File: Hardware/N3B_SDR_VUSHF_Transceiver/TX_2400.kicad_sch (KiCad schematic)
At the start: 123 parts, among them J1 PATCH01, J2 ADF4360+AD8346 SHIELD, J3 SP5189 SHIELD, J4 PATCH02, J5 Line In/PTT, J6 MIC/PTT, J7 SMA RF OUT, SW1 RESET, U1 RP2040_PICO, U2 LM324, U3 LM4562, U4 LM4562, U5 AD8346ARUZ-REEL7, U6 SPF5189Z, U7 ADF4360-0BCP, U8 LM1117-5.0, U9 LM1117-3.3, Y1 10Mhz

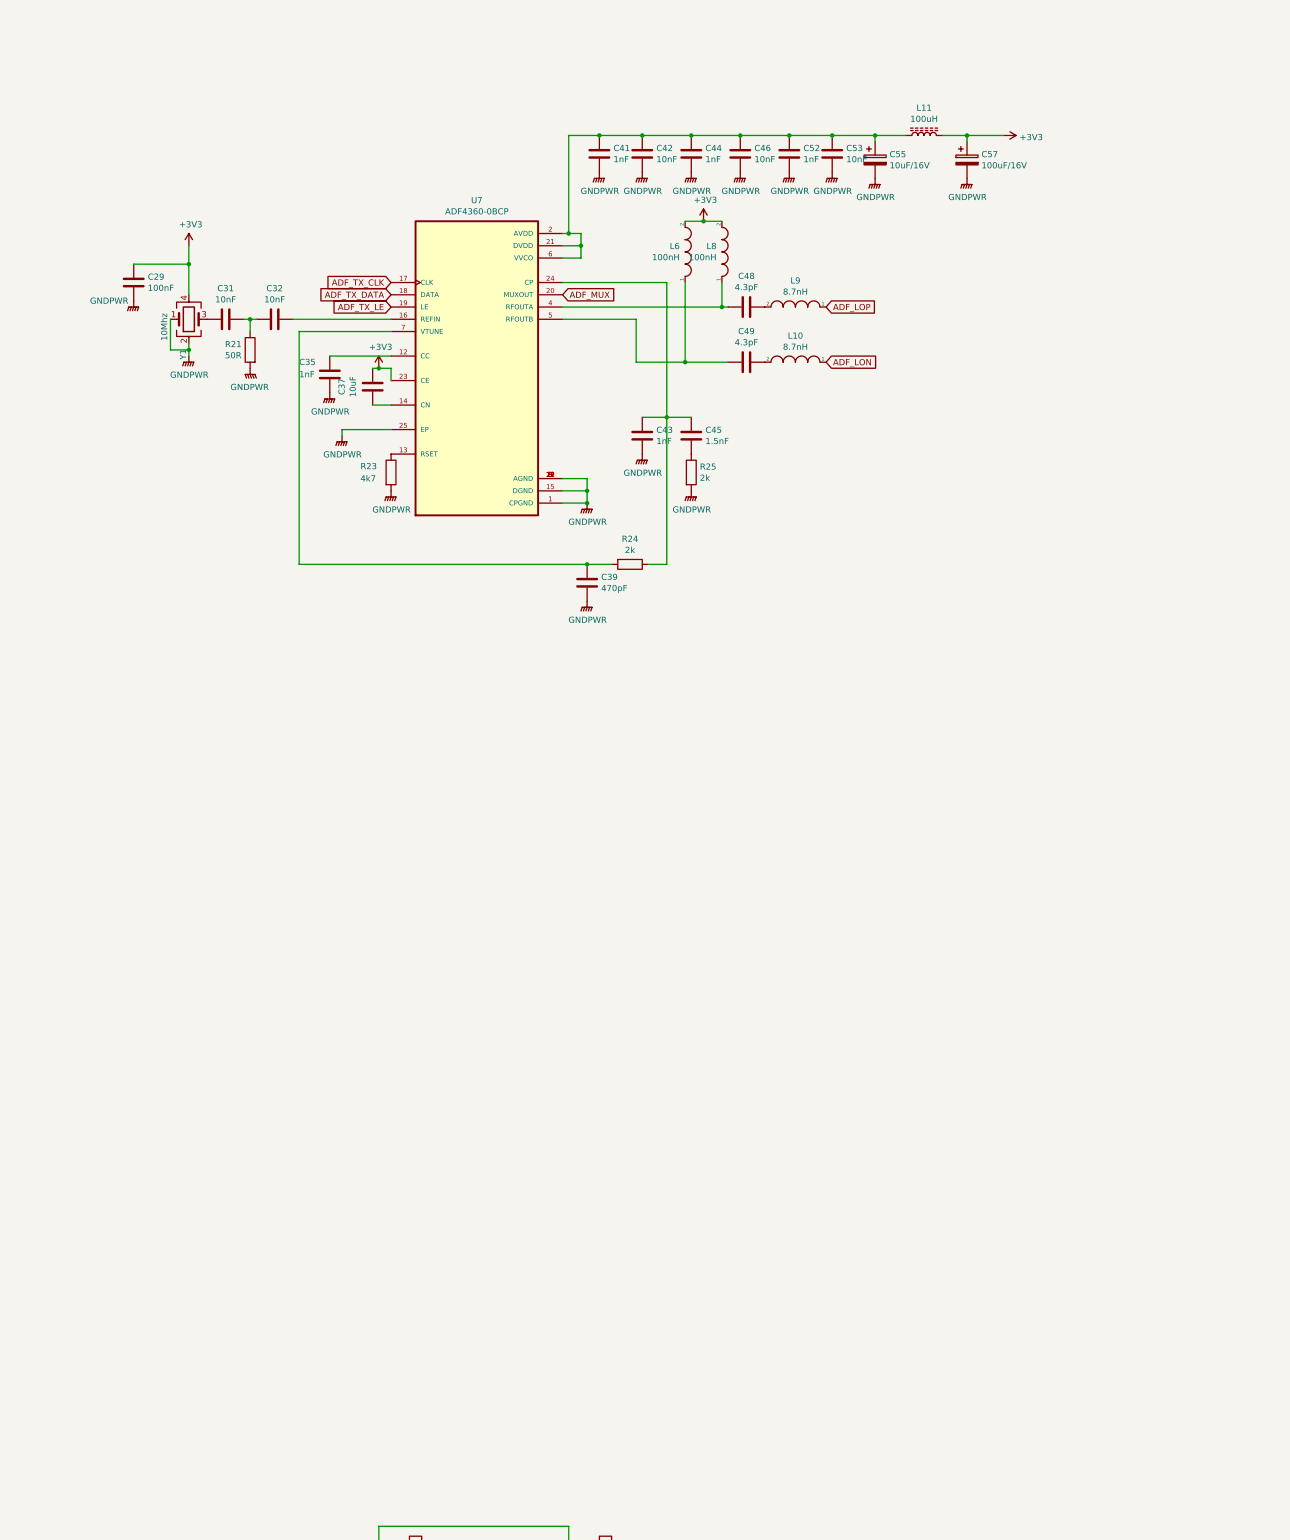
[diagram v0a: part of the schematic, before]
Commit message: TX Synth modified to LMX2581
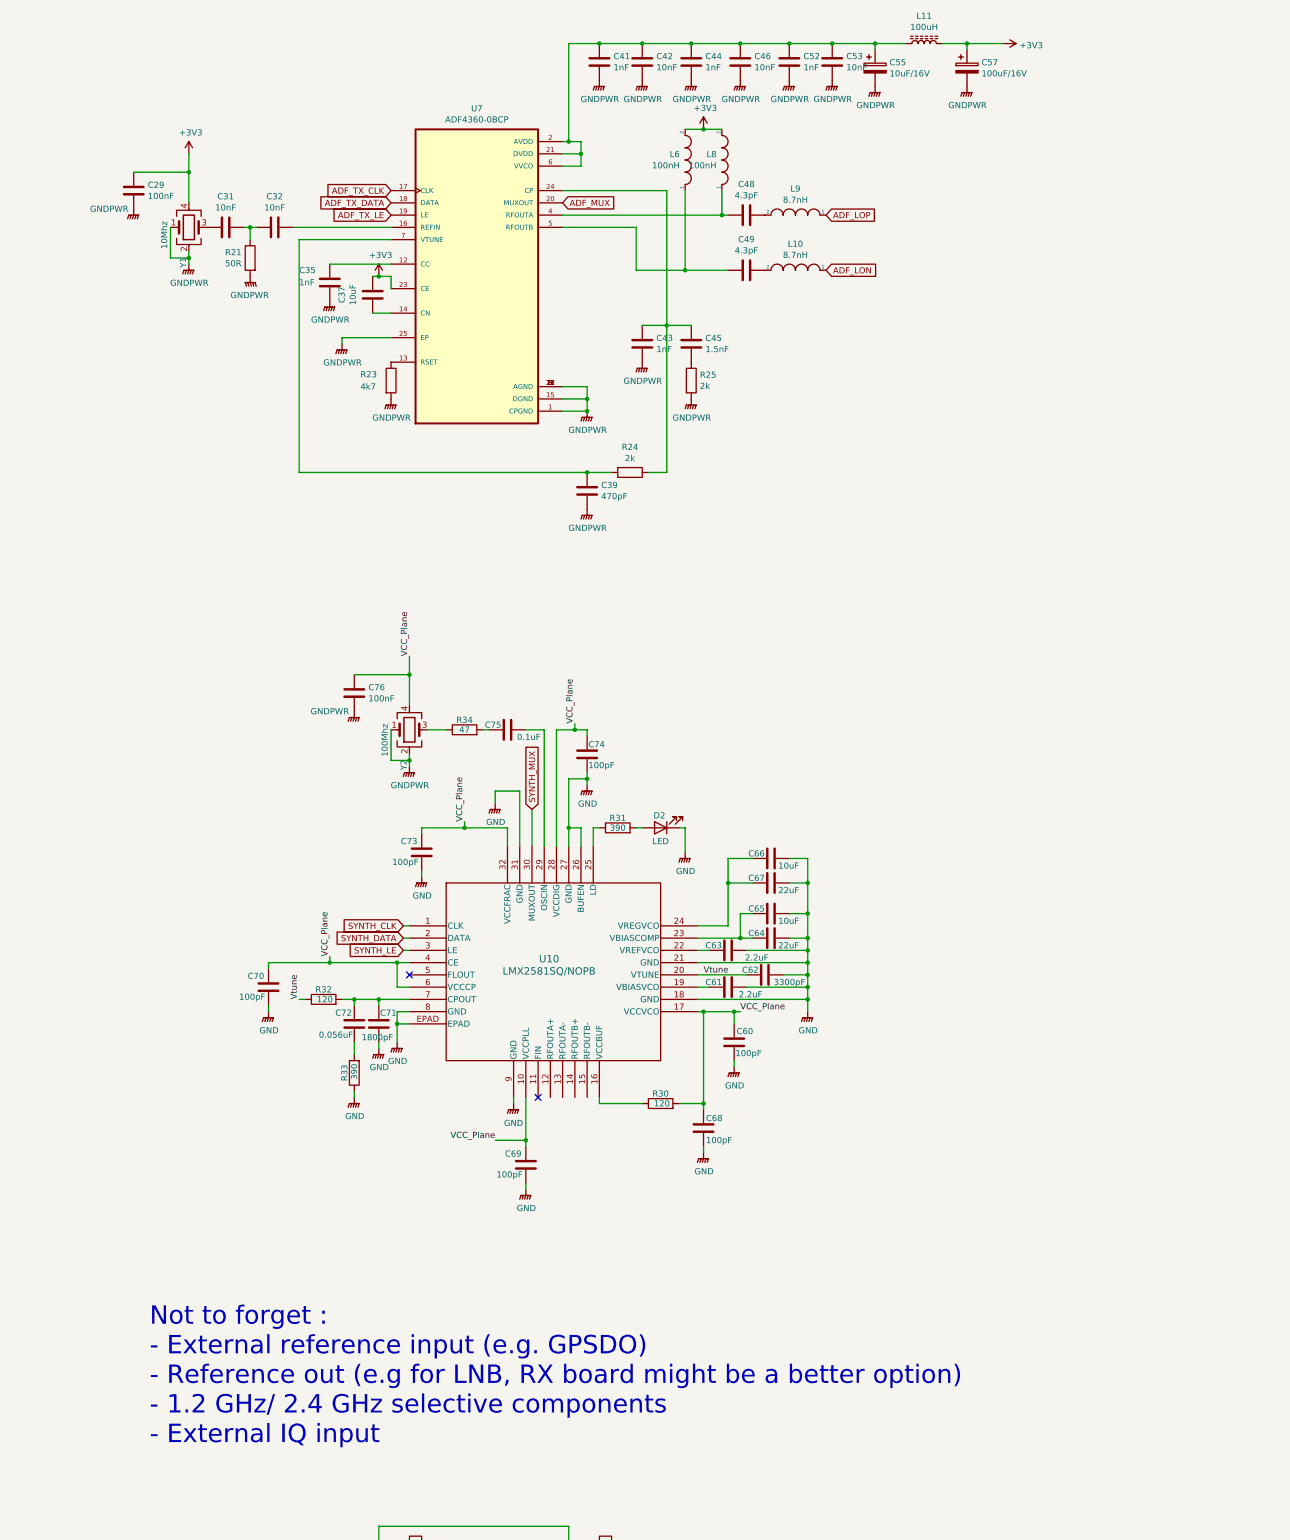
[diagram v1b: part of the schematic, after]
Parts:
- added C60, C68, C69, C70, C73, C74: 100pF, Capacitor_SMD:C_0805_2012Metric, symbol Device:C
- added C61, C63: 2.2uF, Capacitor_SMD:C_0805_2012Metric, symbol Device:C
- added C62: 3300pF, Capacitor_SMD:C_0805_2012Metric, symbol Device:C
- added C64, C67: 22uF, Capacitor_SMD:C_0805_2012Metric, symbol Device:C
- added C65, C66: 10uF, Capacitor_SMD:C_0805_2012Metric, symbol Device:C
- added C71: 1800pF, Capacitor_SMD:C_0805_2012Metric, symbol Device:C
- added C72: 0.056uF, Capacitor_SMD:C_0805_2012Metric, symbol Device:C
- added C75: 0.1uF, Capacitor_SMD:C_0805_2012Metric, symbol Device:C
- added C76: 100nF, Capacitor_SMD:C_0805_2012Metric, symbol Device:C
- added D2: LED, symbol Device:LED
- added R30, R32: 120, Resistor_SMD:R_0805_2012Metric, symbol Device:R
- added R31, R33: 390, Resistor_SMD:R_0805_2012Metric, symbol Device:R
- added R34: 47, Resistor_SMD:R_0805_2012Metric, symbol Device:R
- added U10: LMX2581SQ/NOPB, footprints:LMX2581, symbol LMX2581:LMX2581SQ_NOPB
- added Y2: 100Mhz, Crystal:Crystal_SMD_SeikoEpson_FA238V-4Pin_3.2x2.5mm, symbol Device:Crystal_GND24
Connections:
- net GNDPWR: now also C76.2, Y2.1, Y2.2
- new net: R30.1, U10.16 (VCCBUF)
- new net: C61.1, U10.19 (VBIASVCO)
- new net: C63.1, U10.22 (VREFVCO)
- new net: C64.1, C65.1, U10.23 (VBIASCOMP)
- new net: C66.1, C67.1, U10.24 (VREGVCO)
- new net: R31.1, U10.25 (LD)
- new net: C75.2, U10.29 (OSCIN)
- new net: C71.1, C72.1, R32.2, U10.7 (CPOUT)
- new net: R34.1, Y2.3
- new net: C75.1, R34.2
- new net: C72.2, R33.2
- new net: D2.2 (A), R31.2
- new net GND: C60.2, C61.2, C62.2, C63.2, C64.2, C65.2, C66.2, C67.2, C68.2, C69.2, C70.2, C71.2, C73.2, C74.2, D2.1 (K), R33.1, U10.18 (GND), U10.21 (GND), U10.26 (BUFEN), U10.27 (GND), U10.31 (GND), U10.8 (GND), U10.9 (GND), U10.EPAD
- new net SYNTH_CLK: U10.1 (CLK)
- new net SYNTH_DATA: U10.2 (DATA)
- new net SYNTH_LE: U10.3 (LE)
- new net SYNTH_MUX: U10.30 (MUXOUT)
- new net VCC_Plane: C60.1, C68.1, C69.1, C70.1, C73.1, C74.1, C76.1, R30.2, U10.10 (VCCPLL), U10.17 (VCCVCO), U10.28 (VCCDIG), U10.32 (VCCFRAC), U10.4 (CE), U10.6 (VCCCP), Y2.4
- new net Vtune: C62.1, R32.1, U10.20 (VTUNE)
- no-connect marks 0 -> 2
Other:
- note added: "Not to forget : - External reference input (e.g. GPSDO) - Reference out (e.g for LNB, RX board might be a better option) - 1.2 GHz/ 2.4 GHz selective components - External IQ input"
- moved on the sheet: C29, C31, C32, C35, C37, C39, C41, C42, C43, C44, C45, C46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

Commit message: local oscillators replaced with TI
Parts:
- removed C32, C42, C46: 10nF, Capacitor_SMD:C_0805_2012Metric, symbol Device:C
- removed C35, C41, C43, C44: 1nF, Capacitor_SMD:C_0805_2012Metric, symbol Device:C
- removed C37: 10uF, Capacitor_SMD:C_0805_2012Metric, symbol Device:C
- removed C39: 470pF, Capacitor_SMD:C_0805_2012Metric, symbol Device:C
- removed C45: 1.5nF, Capacitor_SMD:C_0805_2012Metric, symbol Device:C
- removed C48, C49: 4.3pF, Capacitor_SMD:C_0805_2012Metric, symbol Device:C
- removed L10, L9: 8.7nH, Inductor_SMD:L_0603_1608Metric, symbol QO100_TX-rescue:INDUCTOR-pspice
- removed L6, L8: 100nH, Inductor_SMD:L_0603_1608Metric, symbol QO100_TX-rescue:INDUCTOR-pspice
- removed R25: 2k, Resistor_SMD:R_0805_2012Metric, symbol Device:R
- removed U7: ADF4360-0BCP, ADF4360-5BCP:ADF4360SEDA, symbol QO100_TX-rescue:ADF4360-5BCP-ADF4360-5BCP
- removed Y1: 10Mhz, Crystal:Crystal_SMD_SeikoEpson_FA238V-4Pin_3.2x2.5mm, symbol Device:Crystal_GND24
- added J8: SMA REF IN, Connector_Coaxial:SMA_Samtec_SMA-J-P-X-ST-EM1_EdgeMount, symbol Connector:Conn_Coaxial
- added JP1: ~, symbol Jumper:Jumper_2_Bridged
- added JP2: ~, symbol Jumper:Jumper_2_Open
- C29: value 100nF -> 10pF
- C31: value 10nF -> 10pF
- C76: value 100nF -> 1uF
- R21: value 50R -> 10
- R23: value 4k7 -> 18
- R24: value 2k -> 33
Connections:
- net ADF_MUX is gone; now on net SYNTH_MUX: U1.6 (GP4)
- net ADF_TX_CLK is gone; now on net SYNTH_CLK: U1.14 (GP10)
- net ADF_TX_DATA is gone; now on net SYNTH_DATA: U1.15 (GP11)
- net ADF_TX_LE is gone; now on net SYNTH_LE: U1.17 (GP13)
- net +3V3: no longer C29.1
- net GNDPWR: now also J8.2 (Ext); no longer C29.2, R21.2, R23.2
- net VCC_Plane: now also C52.1, C53.1, C55.1, L11.1, R21.2; no longer C76.1, Y2.4
- net at C31.1: now also U10.13 (RFOUTA-)
- net at R23.1: now also R24.1, R34.2
- net at R24.2: now also C75.1
- net at R21.1: now also C76.1, Y2.4; no longer C31.2
- net at U10.12 (RFOUTA+): now also C29.1
- net at Y2.3: now also JP1.1 (A); no longer R34.1
- net ADF_LON renamed LO_N
- net LO_N: now also C31.2
- net ADF_LOP renamed LO_P
- net LO_P: now also C29.2
- new net: J8.1 (In), JP2.2 (B)
- new net: JP1.2 (B), R34.1
- new net: JP2.1 (A), R23.2
- no-connect marks 2 -> 4
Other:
- note added: "Not to forget : - Reference out (e.g for LNB, RX board might be a better option) - 1.2 GHz/ 2.4 GHz selective components - External IQ input"
- note removed: "Not to forget : - External reference input (e.g. GPSDO) - Reference out (e.g for LNB, RX board might be a better option) - 1.2 GHz/ 2.4 GHz selective components - External IQ input"
- moved on the sheet: C52, C53, C55, C57, C60, C61, C62, C63, C64, C65, C66, C67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
